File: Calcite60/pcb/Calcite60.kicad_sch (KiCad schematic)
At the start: 56 parts, among them J1 USB_C_Receptacle_USB2.0, J2 Conn_01x02, J3 Conn_01x02, J4 Conn_01x02, J4 Conn_02x05_Counter_Clockwise, J5 Conn_01x02, J6 Conn_01x04, Q1 AO3407, SW1 SW_DPDT_x2, U1 SRV05-4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

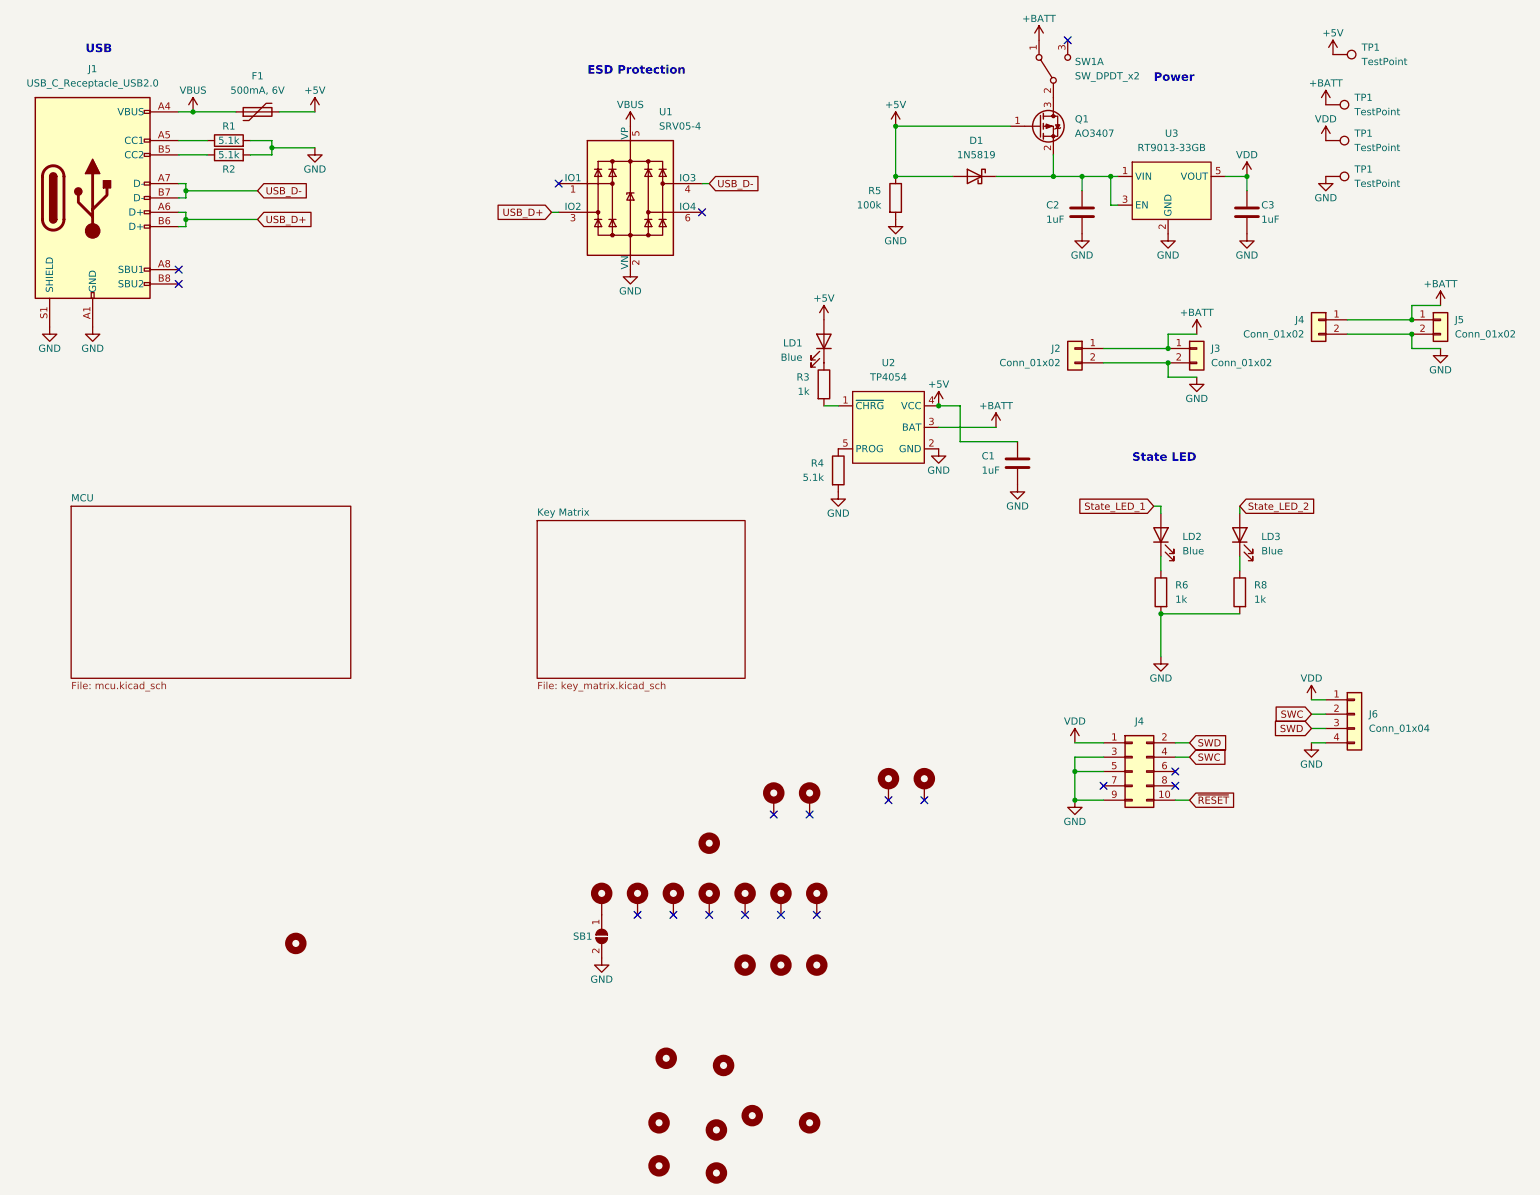
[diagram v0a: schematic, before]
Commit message: Update switch footprint from TS-1064S to TS1064SA
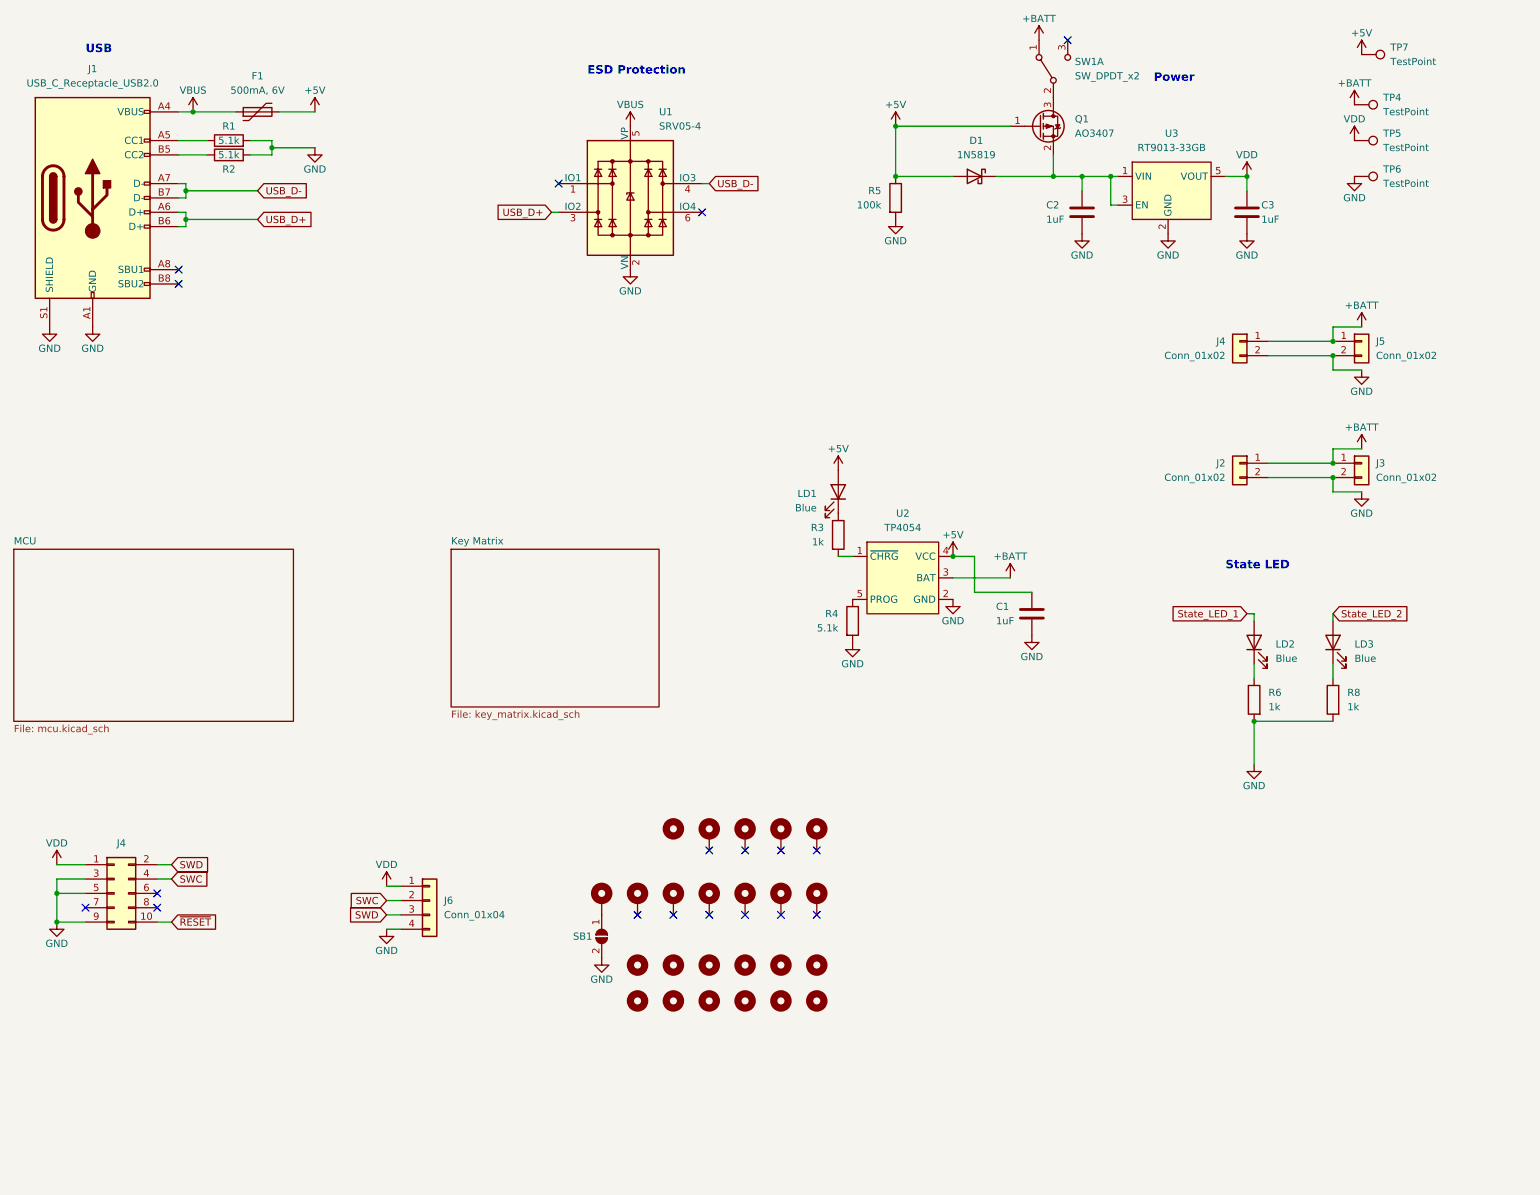
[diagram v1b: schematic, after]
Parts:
- renumbered TP1 to TP4, TP1 to TP5, TP1 to TP6, TP1 to TP7
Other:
- moved on the sheet: C1, J2, J3, J4, J5, J6, LD1, LD2, LD3, R3, R4, R6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

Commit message: Update BOM
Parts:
- C1, C2, C3: LCSC C52923 -> C15849; MFR. Part # CL05A105KA5NQNC -> CL10A105KB8NNNC
- D1: LCSC (none) -> C191023; MFR. Part # (none) -> 1N5819WS
- Q1: LCSC (none) -> C347478; MFR. Part # (none) -> AO3407A
- R1, R2: LCSC C25905 -> C23186; MFR. Part # 0402WGF5101TCE -> 0603WAF5101T5E
- R3, R6, R8: LCSC C11702 -> C21190; MFR. Part # 0402WGF1001TCE -> 0603WAF1001T5E
- R4: LCSC C11702 -> C23186; MFR. Part # 0402WGF1001TCE -> 0603WAF5101T5E
- R5: LCSC C11702 -> C25803; MFR. Part # 0402WGF1001TCE -> 0603WAF1003T5E
- U2: LCSC (none) -> C32574; MFR. Part # (none) -> TP4054-42-SOT25R
- renumbered J4 to J7
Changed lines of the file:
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@@
 (kicad_sch
-	(version 20231120)
+	(version 20250114)
 	(generator "eeschema")
-	(generator_version "8.0")
+	(generator_version "9.0")
 	(paper "A4")
 	(title_block
@@
 		(comment 2 "Kailh Choc V1 (PG1350) Low Profile Switches")
 	)
+	(text "ESD Protection"
+		(exclude_from_sim no)
+		(at 130.81 31.75 0)
+		(effects
+			(font
+				(size 1.5 1.5)
+				(thickness 0.3)
+				(bold yes)
+			)
+			(justify left bottom)
+		)
+	)
+	(text "State LED"
+		(exclude_from_sim no)
+		(at 243.84 119.38 0)
+		(effects
+			(font
+				(size 1.5 1.5)
+				(thickness 0.3)
+				(bold yes)
+			)
+			(justify left bottom)
+		)
+	)
+	(text "USB"
+		(exclude_from_sim no)
+		(at 41.91 27.94 0)
+		(effects
+			(font
+				(size 1.5 1.5)
+				(thickness 0.3)
+				(bold yes)
+			)
+			(justify left bottom)
+		)
+	)
+	(text "Power\n"
+		(exclude_from_sim no)
+		(at 231.14 33.02 0)
+		(effects
+			(font
+				(size 1.5 1.5)
+				(thickness 0.3)
+				(bold yes)
+			)
+			(justify left bottom)
+		)
+	)
 	(junction
 		(at 262.89 81.28)
@@
 		)
 	)
-	(text "ESD Protection"
-		(exclude_from_sim no)
-		(at 130.81 31.75 0)
-		(effects
-			(font
-				(size 1.5 1.5)
-				(thickness 0.3)
-				(bold yes)
-			)
-			(justify left bottom)
-		)
-	)
-	(text "State LED"
-		(exclude_from_sim no)
-		(at 243.84 119.38 0)
-		(effects
-			(font
-				(size 1.5 1.5)
-				(thickness 0.3)
-				(bold yes)
-			)
-			(justify left bottom)
-		)
-	)
-	(text "USB"
-		(exclude_from_sim no)
-		(at 41.91 27.94 0)
-		(effects
-			(font
-				(size 1.5 1.5)
-				(thickness 0.3)
-				(bold yes)
-			)
-			(justify left bottom)
-		)
-	)
-	(text "Power\n"
-		(exclude_from_sim no)
-		(at 231.14 33.02 0)
-		(effects
-			(font
-				(size 1.5 1.5)
-				(thickness 0.3)
-				(bold yes)
-			)
-			(justify left bottom)
-		)
-	)
 	(global_label "SWC"
 		(shape input)
@@
 			)
 		)
-		(property "MFR. Part #" "0402WGF1001TCE "
+		(property "MFR. Part #" "0603WAF1001T5E"
 			(at 262.89 142.24 0)
 			(effects
@@
 			)
 		)
-		(property "LCSC" "C11702"
+		(property "LCSC" "C21190"
 			(at 262.89 142.24 0)
 			(effects
@@
 			)
 		)
-		(property "MFR. Part #" "0402WGF1001TCE "
+		(property "MFR. Part #" "0603WAF5101T5E"
 			(at 177.8 128.27 0)
 			(effects
@@
 			)
 		)
-		(property "LCSC" "C11702"
+		(property "LCSC" "C23186"
 			(at 177.8 128.27 0)
 			(effects
@@
 		(on_board yes)
 		(dnp no)
-		(property "Reference" "J4"
+		(property "Reference" "J7"
 			(at 48.26 167.64 0)
 			(effects
@@
 		(on_board yes)
 		(dnp no)
-		(property "Reference" "#PWR018"
+		(property "Reference" "#PWR038"
 			(at 36.83 187.96 0)
 			(effects
@@
 			)
 		)
-		(property "MFR. Part #" "0402WGF1001TCE "
+		(property "MFR. Part #" "0603WAF1001T5E"
 			(at 248.92 142.24 0)
 			(effects
@@
 			)
 		)
-		(property "LCSC" "C11702"
+		(property "LCSC" "C21190"
 			(at 248.92 142.24 0)
 			(effects
@@
 			)
 		)
-		(property "MFR. Part #" "0402WGF5101TCE"
+		(property "MFR. Part #" "0603WAF5101T5E"
 			(at 67.31 45.72 0)
 			(effects
@@
 			)
 		)
-		(property "LCSC" "C25905"
+		(property "LCSC" "C23186"
 			(at 67.31 45.72 0)
 			(effects
@@
 			)
 		)
-		(property "MFR. Part #" "CL05A105KA5NQNC"
+		(property "MFR. Part #" "CL10A105KB8NNNC"
 			(at 209.55 127 0)
 			(effects
@@
 			)
 		)
-		(property "LCSC" "C52923"
+		(property "LCSC" "C15849"
 			(at 209.55 127 0)
 			(effects
@@
 			)
 		)
+		(property "LCSC" "C347478"
+			(at 210.82 40.64 0)
+			(effects
+				(font
+					(size 1.27 1.27)
+				)
+			)
+		)
+		(property "MFR. Part #" "AO3407A"
+			(at 210.82 40.64 0)
+			(effects
+				(font
+					(size 1.27 1.27)
+				)
+			)
+		)
 		(pin "1"
 		)
@@
 			)
 		)
-		(property "MFR. Part #" "0402WGF1001TCE "
+		(property "MFR. Part #" "0603WAF1003T5E"
 			(at 185.42 53.34 0)
 			(effects
@@
 			)
 		)
-		(property "LCSC" "C11702"
+		(property "LCSC" "C25803"
 			(at 185.42 53.34 0)
 			(effects
@@
 			)
 		)
+		(property "LCSC" "C191023"
+			(at 199.39 49.53 0)
+			(effects
+				(font
+					(size 1.27 1.27)
+				)
+			)
+		)
+		(property "MFR. Part #" "1N5819WS"
+			(at 199.39 49.53 0)
+			(effects
+				(font
+					(size 1.27 1.27)
+				)
+			)
+		)
 		(pin "1"
 		)
@@
 			)
 		)
-		(property "MFR. Part #" "CL05A105KA5NQNC"
+		(property "MFR. Part #" "CL10A105KB8NNNC"
 			(at 247.65 55.88 0)
 			(effects
@@
 			)
 		)
-		(property "LCSC" "C52923"
+		(property "LCSC" "C15849"
 			(at 247.65 55.88 0)
 			(effects
@@
 			)
 		)
-		(property "MFR. Part #" "0402WGF1001TCE "
+		(property "MFR. Part #" "0603WAF1001T5E"
 			(at 175.26 113.03 0)
 			(effects
@@
 			)
 		)
-		(property "LCSC" "C11702"
+		(property "LCSC" "C21190"
 			(at 175.26 113.03 0)
 			(effects
@@
 			)
 		)
-		(property "MFR. Part #" "0402WGF5101TCE"
+		(property "MFR. Part #" "0603WAF5101T5E"
 			(at 67.31 43.18 0)
 			(effects
@@
 			)
 		)
-		(property "LCSC" "C25905"
+		(property "LCSC" "C23186"
 			(at 67.31 43.18 0)
 			(effects
@@
 			)
 		)
+		(property "LCSC" "C32574"
+			(at 186.69 120.65 0)
+			(effects
+				(font
+					(size 1.27 1.27)
+				)
+			)
+		)
+		(property "MFR. Part #" "TP4054-42-SOT25R"
+			(at 186.69 120.65 0)
+			(effects
+				(font
+					(size 1.27 1.27)
+				)
+			)
+		)
 		(pin "1"
 		)
@@
 			)
 		)
-		(property "MFR. Part #" "CL05A105KA5NQNC"
+		(property "MFR. Part #" "CL10A105KB8NNNC"
 			(at 218.44 55.88 0)
 			(effects
@@
 			)
 		)
-		(property "LCSC" "C52923"
+		(property "LCSC" "C15849"
 			(at 218.44 55.88 0)
 			(effects
@@
 		(at 29.21 115.57)
 		(size 49.53 30.48)
+		(exclude_from_sim no)
+		(in_bom yes)
+		(on_board yes)
+		(dnp no)
 		(fields_autoplaced yes)
 		(stroke
@@
 		(at 106.68 115.57)
 		(size 36.83 27.94)
+		(exclude_from_sim no)
+		(in_bom yes)
+		(on_board yes)
+		(dnp no)
 		(fields_autoplaced yes)
 		(stroke
@@
 		)
 	)
+	(embedded_fonts no)
 )
